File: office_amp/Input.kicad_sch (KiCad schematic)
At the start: 25 parts, among them J2 Conn_01x03_Female, J3 Conn_02x07_Odd_Even, J8 Conn_01x03_Female, K1 V23079-A1003-B301, K2 V23079-A1003-B301, K3 V23079-A1003-B301, K4 V23079-A1003-B301, Q4 BC850, Q5 BC850, U5 MH-M18

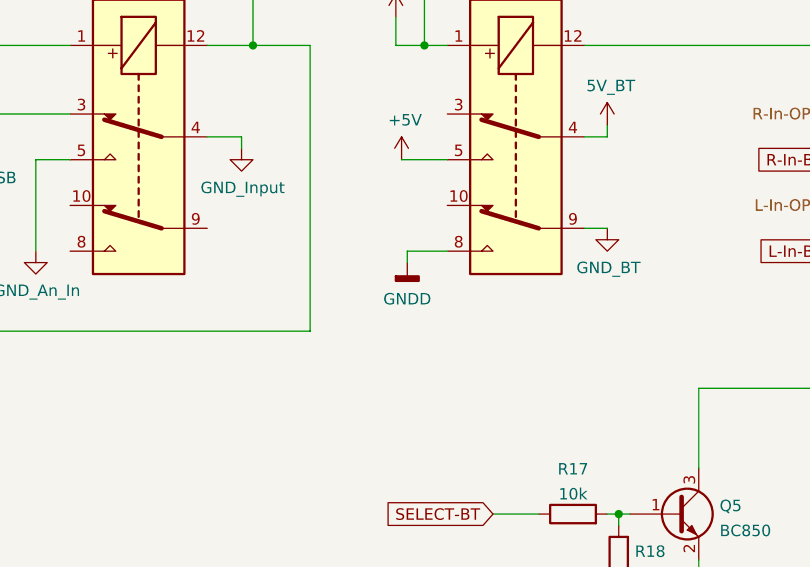
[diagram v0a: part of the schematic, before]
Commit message: removed errors control board, added interrupt pins controllboard
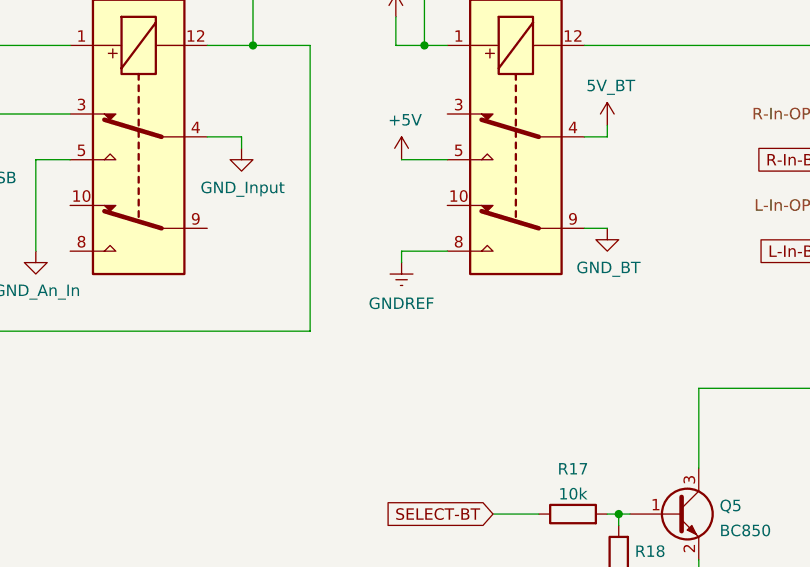
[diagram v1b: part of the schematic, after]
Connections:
- net GNDD: no longer K3.8
- net GNDREF: now also K3.8
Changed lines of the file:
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@@
+    (stroke (width 0) (type default) (color 0 0 0 0))
+  )
+  (wire (pts (xy 193.04 64.77) (xy 193.04 63.5))
     (stroke (width 0) (type default) (color 0 0 0 0))
   )
@@
     (stroke (width 0) (type default) (color 0 0 0 0))
   )
-  (wire (pts (xy 193.675 64.77) (xy 193.675 63.5))
-    (stroke (width 0) (type default) (color 0 0 0 0))
-  )
   (wire (pts (xy 140.97 158.75) (xy 146.05 158.75))
     (stroke (width 0) (type default) (color 0 0 0 0))
@@
     (stroke (width 0) (type default) (color 0 0 0 0))
   )
+  (wire (pts (xy 193.04 63.5) (xy 198.12 63.5))
+    (stroke (width 0) (type default) (color 0 0 0 0))
+  )
   (wire (pts (xy 266.7 93.98) (xy 270.51 93.98))
     (stroke (width 0) (type default) (color 0 0 0 0))
@@
   )
   (wire (pts (xy 213.36 60.96) (xy 215.9 60.96))
-    (stroke (width 0) (type default) (color 0 0 0 0))
-  )
-  (wire (pts (xy 193.675 63.5) (xy 198.12 63.5))
     (stroke (width 0) (type default) (color 0 0 0 0))
   )
@@
     (pin "3")
   )
-  (symbol (lib_id "power:GNDD") (at 193.675 64.77 0) (unit 1)
-    (in_bom yes) (on_board yes) (fields_autoplaced)
-    (property "Reference" "#PWR021" (id 0) (at 193.675 71.12 0)
-      (effects (font (size 1.27 1.27)) hide)
-    )
-    (property "Value" "GNDD" (id 1) (at 193.675 68.8324 0))
-    (property "Footprint" "" (id 2) (at 193.675 64.77 0)
-      (effects (font (size 1.27 1.27)) hide)
-    )
-    (property "Datasheet" "" (id 3) (at 193.675 64.77 0)
-      (effects (font (size 1.27 1.27)) hide)
-    )
-    (pin "1")
-  )
   (symbol (lib_id "power:GNDD") (at 146.05 161.29 0) (unit 1)
     (in_bom yes) (on_board yes) (fields_autoplaced)
@@
       (effects (font (size 1.27 1.27)) hide)
     )
+    (pin "1")
+  )
+  (symbol (lib_id "power:GNDREF") (at 193.04 64.77 0) (unit 1)
+    (in_bom yes) (on_board yes) (fields_autoplaced)
+    (property "Reference" "#PWR?" (id 0) (at 193.04 71.12 0)
+      (effects (font (size 1.27 1.27)) hide)
+    )
+    (property "Value" "GNDREF" (id 1) (at 193.04 69.3325 0))
+    (property "Footprint" "" (id 2) (at 193.04 64.77 0)
+      (effects (font (size 1.27 1.27)) hide)
+    )
+    (property "Datasheet" "" (id 3) (at 193.04 64.77 0)
+      (effects (font (size 1.27 1.27)) hide)
+    )
